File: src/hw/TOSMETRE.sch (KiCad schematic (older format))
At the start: 20 parts, among them J1 Alim, J2 Conn_Coaxial, J3 PRG PIC, J4 LCD 4x20, J5 Conn_Coaxial, U1 18F1320, U2 L7805, U3 MAX4624, U4 MAX11100

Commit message: suppression U3 et U4 #155
suppression U3 et U4 #155
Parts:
- removed U3: MAX4624, Package_TO_SOT_SMD:SOT-23-6, symbol TOSMETRE-rescue:MAX4624-16F88
- removed U4: MAX11100, Package_SO:MSOP-10_3x3mm_P0.5mm, symbol TOSMETRE-rescue:MAX11100-16F88
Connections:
- wire segments 107 -> 76
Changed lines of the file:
@@
 Wire Wire Line
 	8150 1150 9800 1150
-$Comp
-L TOSMETRE-rescue:MAX11100-16F88 U4
-U 1 1 5CFD76E0
-P 5400 2250
-F 0 "U4" V 5917 2577 50  0000 L CNN
-F 1 "MAX11100" V 5995 2457 50  0000 L CNN
-F 2 "Package_SO:MSOP-10_3x3mm_P0.5mm" V 6050 2600 50  0001 C CNN
-F 3 "" V 5100 2550 50  0001 C CNN
-	1    5400 2250
-	0    1    1    0
-$EndComp
 Connection ~ 8150 1150
 Wire Wire Line
@@
 Wire Wire Line
 	8350 3150 8350 3600
-Text Notes 4700 2500 0    50   ~ 0
+Text Notes 4200 1300 0    50   ~ 0
 +5V
 $Comp
@@
 	3800 1150 3450 1150
 Connection ~ 3800 1150
-Wire Wire Line
-	4150 5300 3250 5300
 Connection ~ 4150 1150
 $Comp
@@
 	-1   0    0    1
 $EndComp
-Wire Wire Line
-	4650 2550 4650 2600
-$Comp
-L power:GNDREF #PWR0101
-U 1 1 5E7F5C1D
-P 4650 2600
-F 0 "#PWR0101" H 4650 2350 50  0001 C CNN
-F 1 "GNDREF" H 4655 2427 50  0000 C CNN
-F 2 "" H 4650 2600 50  0001 C CNN
-F 3 "" H 4650 2600 50  0001 C CNN
-	1    4650 2600
-	1    0    0    -1
-$EndComp
 $Comp
 L Device:C C4
@@
 Wire Wire Line
 	6500 1150 6500 1600
-Wire Wire Line
-	6250 2550 6500 2550
 Text Notes 6500 1300 0    50   ~ 0
 +5V
@@
 Wire Wire Line
 	4150 1150 4150 2450
-Connection ~ 4150 2450
-Wire Wire Line
-	4150 2450 4150 5300
-Connection ~ 4600 2450
-Wire Wire Line
-	4600 2450 5300 2450
-$Comp
-L power:GNDREF #PWR0103
-U 1 1 5E82596D
-P 4950 1900
-F 0 "#PWR0103" H 4950 1650 50  0001 C CNN
-F 1 "GNDREF" H 4955 1727 50  0000 C CNN
-F 2 "" H 4950 1900 50  0001 C CNN
-F 3 "" H 4950 1900 50  0001 C CNN
-	1    4950 1900
-	-1   0    0    1
-$EndComp
-Wire Wire Line
-	5300 2350 4950 2350
-Wire Wire Line
-	4950 2350 4950 1900
 Wire Wire Line
 	4600 2150 4600 1900
@@
 Wire Wire Line
 	6500 2650 6800 2650
-Connection ~ 6500 2650
 Wire Wire Line
 	2250 1150 2850 1150
@@
 Wire Wire Line
 	6500 1600 6150 1600
-Wire Wire Line
-	6250 2650 6500 2650
-Wire Wire Line
-	7750 4600 7750 5400
-Connection ~ 6500 1600
-Wire Wire Line
-	6500 1600 6500 2550
-Wire Wire Line
-	3250 5400 7750 5400
-$Comp
-L TOSMETRE-rescue:MAX4624-16F88 U3
-U 1 1 5CFD8181
-P 3150 5400
-F 0 "U3" V 3437 5671 50  0000 C CNN
-F 1 "MAX4624" V 3503 5668 50  0000 C CNN
-F 2 "Package_TO_SOT_SMD:SOT-23-6" V 3650 5650 50  0001 C CNN
-F 3 "" V 3500 5450 50  0001 C CNN
-	1    3150 5400
-	0    -1   -1   0
-$EndComp
-Wire Wire Line
-	2500 5400 1700 5400
 NoConn ~ 8650 4600
 NoConn ~ 8550 4600
@@
 Wire Wire Line
 	8150 1450 8150 3150
-Wire Wire Line
-	6250 2350 7850 2350
-Wire Wire Line
-	7850 2350 7850 3600
-Wire Wire Line
-	6250 2250 7950 2250
-Wire Wire Line
-	7950 2250 7950 3600
-Wire Wire Line
-	5300 2250 5150 2250
-Wire Wire Line
-	5150 2250 5150 2100
-Wire Wire Line
-	5150 2100 8050 2100
-Wire Wire Line
-	8050 2100 8050 3600
-Wire Wire Line
-	6250 2450 7250 2450
-Wire Wire Line
-	7250 2450 7250 2800
-$Comp
-L power:GNDREF #PWR0107
-U 1 1 5EA31A54
-P 7250 2800
-F 0 "#PWR0107" H 7250 2550 50  0001 C CNN
-F 1 "GNDREF" H 7255 2627 50  0000 C CNN
-F 2 "" H 7250 2800 50  0001 C CNN
-F 3 "" H 7250 2800 50  0001 C CNN
-	1    7250 2800
-	1    0    0    -1
-$EndComp
-Wire Wire Line
-	2350 3250 2350 5300
-Wire Wire Line
-	4650 2550 5300 2550
-Wire Wire Line
-	4850 3250 4850 2650
-Wire Wire Line
-	4850 2650 5300 2650
-Wire Wire Line
-	4850 3250 2350 3250
-Wire Wire Line
-	2500 5300 2350 5300
 $Comp
 L Connector:Conn_Coaxial J5
@@
 Wire Wire Line
 	1700 4900 1700 5050
-Wire Wire Line
-	1700 5200 2500 5200
 $Comp
 L power:GNDREF #PWR0111
@@
 Wire Wire Line
 	1900 3850 2100 3850
-Connection ~ 1700 5750
-Wire Wire Line
-	1700 5750 1700 5400
 Wire Wire Line
 	1700 6250 1700 6550
-Connection ~ 1700 5050
-Wire Wire Line
-	1700 5050 1700 5200
 Wire Wire Line
 	1700 4050 1700 4600

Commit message: un peu de nettoyage supplémentaire #155 #118
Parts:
- removed C3, C4, C6: C, Capacitor_SMD:C_1206_3216Metric, symbol Device:C
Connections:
- net GNDREF: no longer C7.1, C8.1, J2.2 (Ext), J5.2 (Ext)
- net at J5.1 (In): no longer D2.2 (A)
- net at J2.1 (In): no longer D3.2 (A)
- net at D3.1 (K): no longer C8.2
- net at D2.1 (K): no longer C7.2
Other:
- note added: "Signal réfléchi"
- note added: "Signal transmis"
- note removed: "FWD"
- note removed: "REF"
- note removed: "VREF"
- moved on the sheet: C7, C8, D2, D3, J2, J5

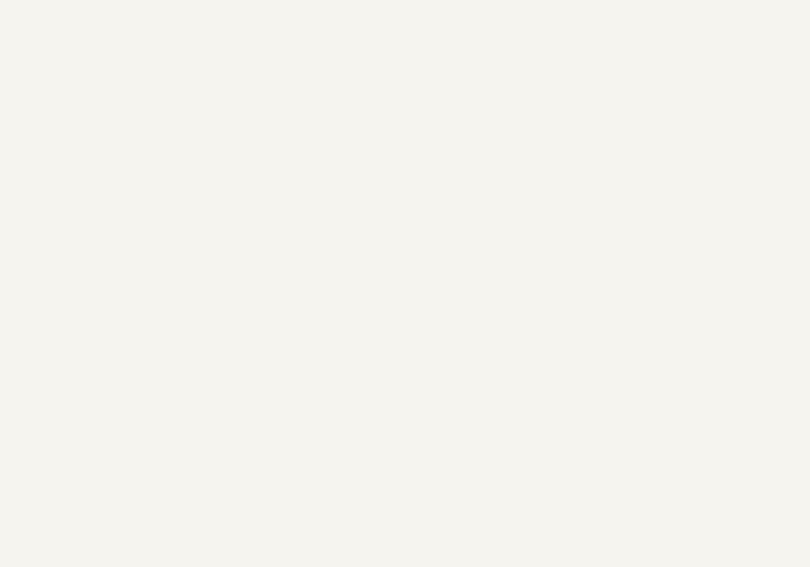
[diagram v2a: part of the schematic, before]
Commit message: pose de l'AD5175
pose de l'AD5175 #164
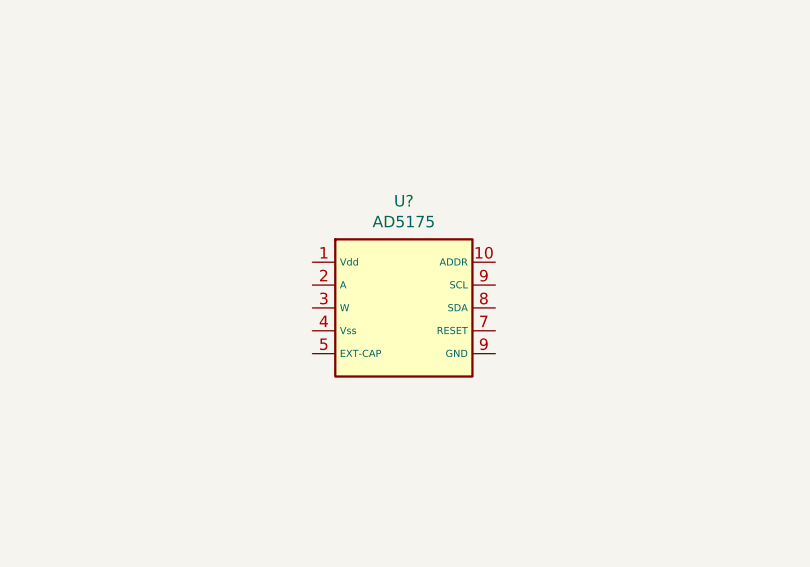
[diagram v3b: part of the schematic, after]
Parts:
- added U?: AD5175, Package_SO:MSOP-10_3x3mm_P0.5mm, symbol librairie_projet:AD5175
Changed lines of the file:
@@
 	-1   0    0    1
 $EndComp
+$Comp
+L librairie_projet:AD5175 U?
+U 1 1 5EB81854
+P 4700 3650
+F 0 "U?" H 4700 4117 50  0000 C CNN
+F 1 "AD5175" H 4700 4026 50  0000 C CNN
+F 2 "Package_SO:MSOP-10_3x3mm_P0.5mm" H 4800 4150 50  0001 C CNN
+F 3 "" H 4700 3650 50  0001 C CNN
+	1    4700 3650
+	1    0    0    -1
+$EndComp
 $EndSCHEMATC

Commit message: Mise en place LT818
mise en place du LT818 #168
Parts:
- added U?: LT818, Package_TO_SOT_SMD:TSOT-23-5, symbol librairie_projet:LT818
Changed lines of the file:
@@
 EESchema Schematic File Version 4
-EELAYER 30 0
+LIBS:TOSMETRE-cache
+EELAYER 29 0
 EELAYER END
 $Descr A4 11693 8268
@@
 	1    0    0    -1
 $EndComp
+$Comp
+L librairie_projet:LT818 U?
+U 1 1 5EBCC901
+P 4200 5000
+F 0 "U?" H 4500 5342 50  0000 C CNN
+F 1 "LT818" H 4500 5251 50  0000 C CNN
+F 2 "Package_TO_SOT_SMD:TSOT-23-5" H 4500 5325 50  0001 C CIN
+F 3 "http://www.st.com/internet/com/TECHNICAL_RESOURCES/TECHNICAL_LITERATURE/DATASHEET/CD00003395.pdf" H 4500 5050 50  0001 C CNN
+	1    4200 5000
+	1    0    0    -1
+$EndComp

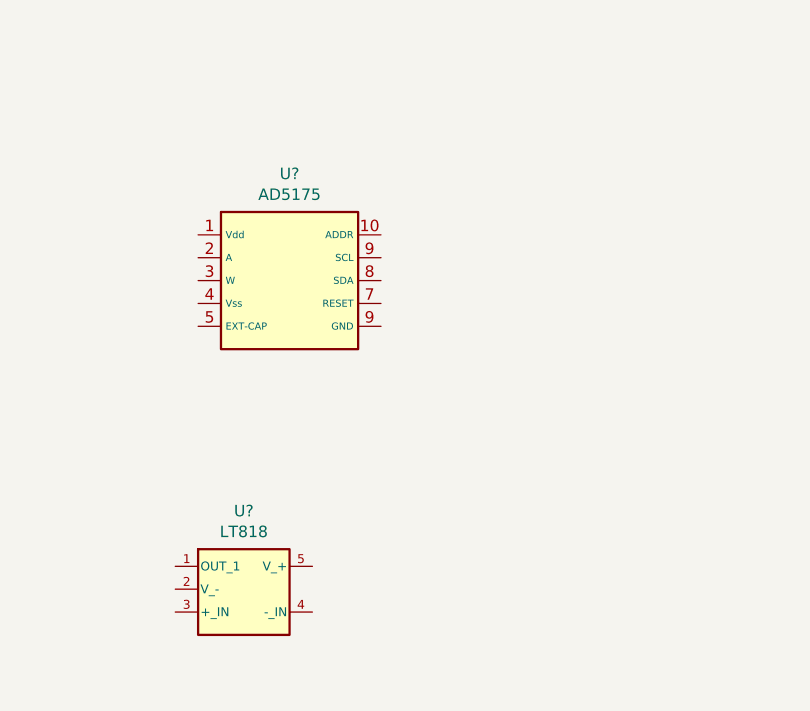
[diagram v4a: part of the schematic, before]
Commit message: renomage et ajout composant
renomage du composant LT818 et LT1818 dans le schema et la librairie
Ajout du AD5175 manquant #191
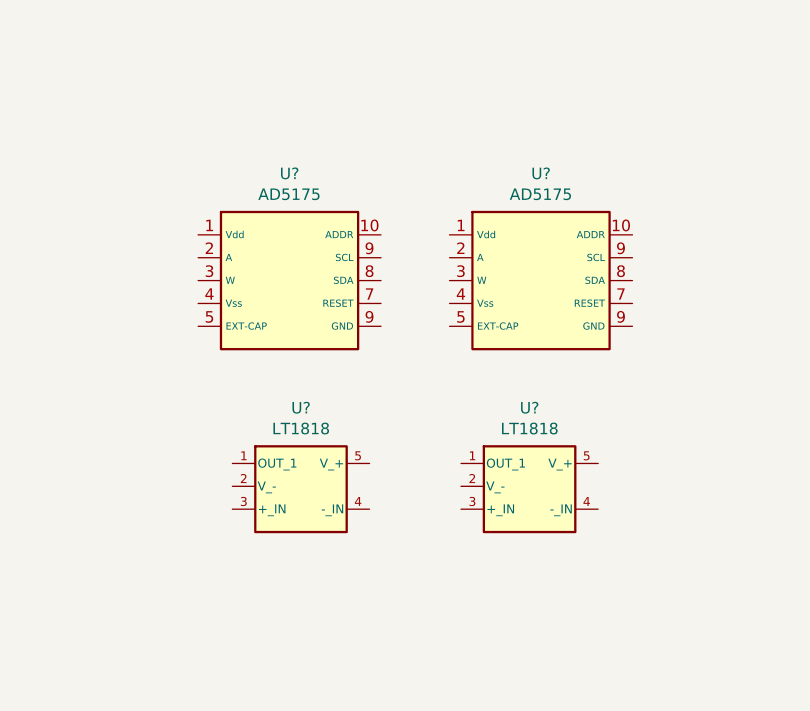
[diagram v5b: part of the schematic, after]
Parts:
- removed U?: LT818, Package_TO_SOT_SMD:TSOT-23-5, symbol librairie_projet:LT818
- added U? (x2): LT1818, Package_TO_SOT_SMD:TSOT-23-5, symbol librairie_projet:LT1818
- added U?: AD5175, Package_SO:MSOP-10_3x3mm_P0.5mm, symbol librairie_projet:AD5175
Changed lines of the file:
@@
 $EndComp
 $Comp
-L librairie_projet:LT818 U?
-U 1 1 5EBCC901
-P 4200 5000
-F 0 "U?" H 4500 5342 50  0000 C CNN
-F 1 "LT818" H 4500 5251 50  0000 C CNN
-F 2 "Package_TO_SOT_SMD:TSOT-23-5" H 4500 5325 50  0001 C CIN
-F 3 "http://www.st.com/internet/com/TECHNICAL_RESOURCES/TECHNICAL_LITERATURE/DATASHEET/CD00003395.pdf" H 4500 5050 50  0001 C CNN
-	1    4200 5000
+L librairie_projet:LT1818 U?
+U 1 1 5EBDCDD4
+P 4450 4550
+F 0 "U?" H 4750 4892 50  0000 C CNN
+F 1 "LT1818" H 4750 4801 50  0000 C CNN
+F 2 "Package_TO_SOT_SMD:TSOT-23-5" H 4750 4875 50  0001 C CIN
+F 3 "http://www.st.com/internet/com/TECHNICAL_RESOURCES/TECHNICAL_LITERATURE/DATASHEET/CD00003395.pdf" H 4750 4600 50  0001 C CNN
+	1    4450 4550
 	1    0    0    -1
 $EndComp
+$Comp
+L librairie_projet:LT1818 U?
+U 1 1 5EBDDABC
+P 5450 4550
+F 0 "U?" H 5750 4892 50  0000 C CNN
+F 1 "LT1818" H 5750 4801 50  0000 C CNN
+F 2 "Package_TO_SOT_SMD:TSOT-23-5" H 5750 4875 50  0001 C CIN
+F 3 "http://www.st.com/internet/com/TECHNICAL_RESOURCES/TECHNICAL_LITERATURE/DATASHEET/CD00003395.pdf" H 5750 4600 50  0001 C CNN
+	1    5450 4550
+	1    0    0    -1
+$EndComp
+$Comp
+L librairie_projet:AD5175 U?
+U 1 1 5EBDF7FE
+P 5800 3650
+F 0 "U?" H 5800 4117 50  0000 C CNN
+F 1 "AD5175" H 5800 4026 50  0000 C CNN
+F 2 "Package_SO:MSOP-10_3x3mm_P0.5mm" H 5900 4150 50  0001 C CNN
+F 3 "" H 5800 3650 50  0001 C CNN
+	1    5800 3650
+	1    0    0    -1
+$EndComp

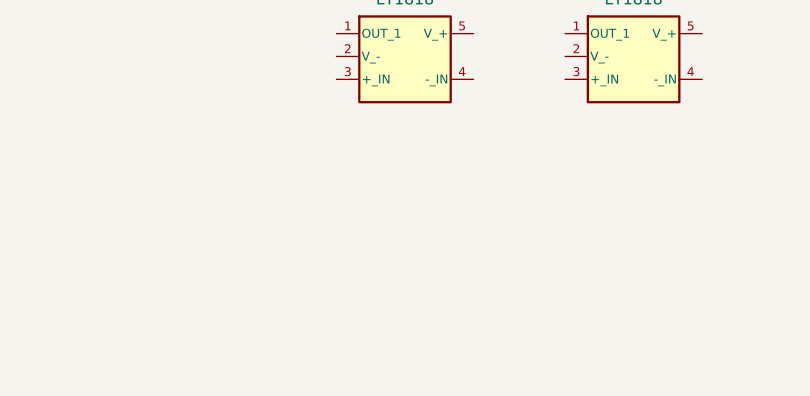
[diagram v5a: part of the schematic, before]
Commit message: mise en place du LTC2305
mise en place du LTC2305 #119
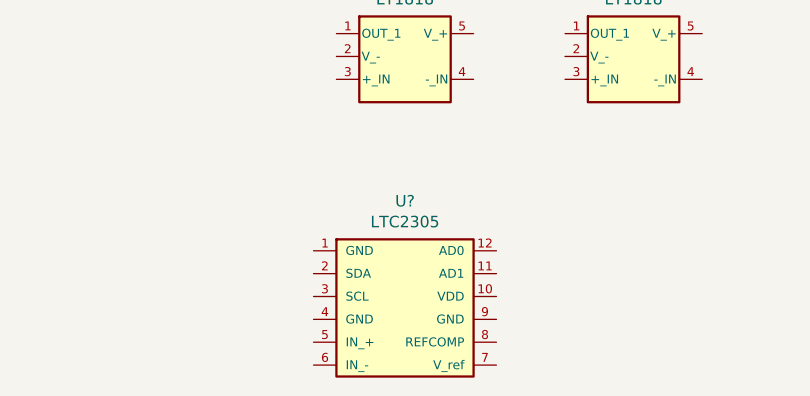
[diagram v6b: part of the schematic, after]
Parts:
- added U?: LTC2305, Package_SO:MSOP-8_3x3mm_P0.65mm, symbol librairie_projet:LTC2305
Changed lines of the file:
@@
 EESchema Schematic File Version 4
-LIBS:TOSMETRE-cache
-EELAYER 29 0
+EELAYER 30 0
 EELAYER END
 $Descr A4 11693 8268
@@
 	1    0    0    -1
 $EndComp
+$Comp
+L librairie_projet:LTC2305 U?
+U 1 1 5EBEB456
+P 4750 5650
+F 0 "U?" H 4750 6117 50  0000 C CNN
+F 1 "LTC2305" H 4750 6026 50  0000 C CNN
+F 2 "Package_SO:MSOP-8_3x3mm_P0.65mm" H 3800 5300 50  0001 C CNN
+F 3 "http://datasheets.maximintegrated.com/en/ds/MAX31826.pdf" H 4550 5500 50  0001 C CNN
+	1    4750 5650
+	1    0    0    -1
+$EndComp

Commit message: RACORDEMENT AD LTC ET LT
PREMIERE VAGUE
#196
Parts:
- added C? (x2): C, Capacitor_SMD:C_1206_3216Metric, symbol Device:C
- added R? (x4): R, symbol Device:R
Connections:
- net GNDREF: now also C?.2, C?.2, R?.1, R?.2
- net at C2.1, C5.1, J4.8 (Pin_8)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: now also U?.1 (Vdd), U?.1 (Vdd)
- net at U?.2 (A): now also U?.4 (-_IN), R?.1
- net at U?.1 (OUT_1): now also R?.1
- net at U?.1 (OUT_1): now also U?.3 (W), R?.2
- net at U?.4 (-_IN): now also U?.2 (A), R?.2
- net at U?.11 (AD1): now also C?.1, R?.2
- net at U?.12 (AD0): now also C?.1, R?.1
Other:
- moved on the sheet: C7, C8, D2, D3, J2, J5, U?

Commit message: Raccordement AD LTC et LT suite
Raccordement AD LTC  et LT #196  mais maintenant je calle grave je me perd
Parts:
- added C? (x2): 1µF, Capacitor_SMD:C_1206_3216Metric, symbol Device:C
- added C? (x2): 10µF, Capacitor_SMD:C_1206_3216Metric, symbol Device:C
- added C? (x2): 100nF, Capacitor_SMD:C_1206_3216Metric, symbol Device:C
- C? (x2): value C -> 2nF
- R? (x2): value R -> 50
- R? (x2): value R -> 25
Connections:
- net GNDREF: now also U?.10 (ADDR), U?.2 (V_-), U?.2 (V_-), C?.1, C?.1, C?.1, C?.1, C?.1, C?.1
- net at C2.1, C5.1, J4.8 (Pin_8)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: now also U?.7 (RESET), U?.7 (RESET), C?.2, C?.2, C?.2, C?.2
- net at U?.5 (EXT-CAP): now also C?.2 (x2)
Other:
- moved on the sheet: C1, C2, C5, C7, C8, C?, D1, D2, D3, J1, J2, J3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
